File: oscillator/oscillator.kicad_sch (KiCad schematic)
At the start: 32 parts, among them SW1 LFO Switch, U1 AS3340-custom, U2 TL074, U3 TL072

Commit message: Improve oscillator bass
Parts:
- C3: value 1nF -> 4.7nF
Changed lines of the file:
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@@
 		)
 	)
-	(text_box "Switch to toggle between an audio frequency oscillator and a low-frequency oscillator."
+	(text_box "Switch to toggle between an audio frequency oscillator and a low-frequency oscillator.\n\nHigher capacitance means a lower frequency. The design this is based off used lower valued capacitors here but I found these values to produce a more useful low-end of the frequency spectrum produced by the oscillator."
 		(exclude_from_sim no)
 		(at 246.38 115.57 0)
-		(size 24.13 12.7)
+		(size 24.13 38.1)
 		(stroke
 			(width 0)
@@
 			)
 		)
-		(property "Value" "1nF"
-			(at 240.03 142.748 90)
+		(property "Value" "4.7nF"
+			(at 240.03 143.51 90)
 			(effects
 				(font

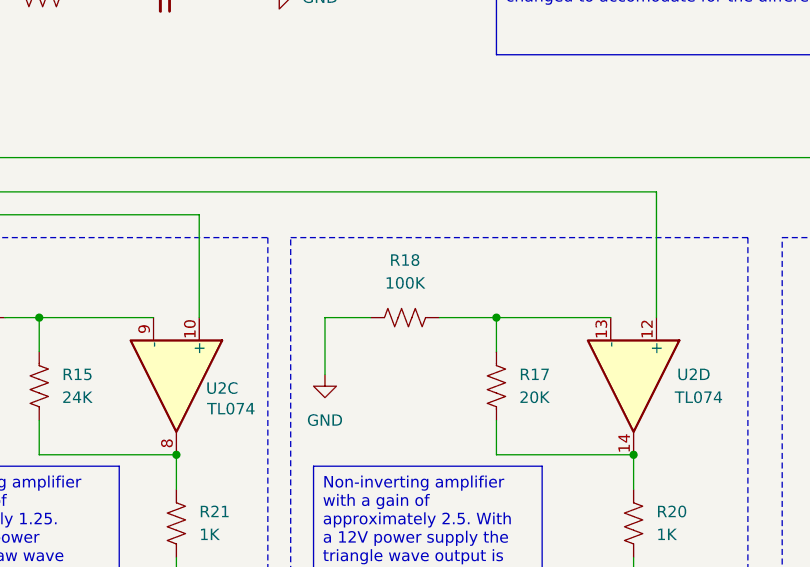
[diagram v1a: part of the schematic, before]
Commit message: Fix typo in oscillator
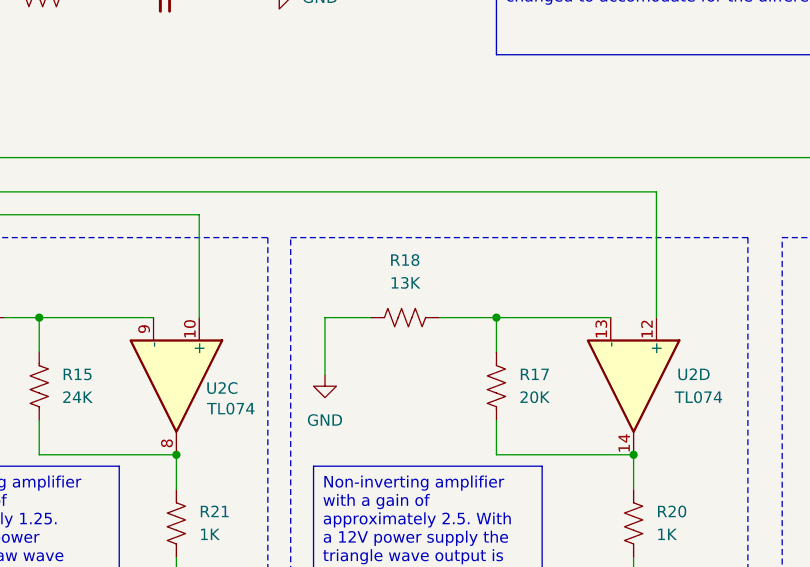
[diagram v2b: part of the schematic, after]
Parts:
- R18: value 100K -> 13K
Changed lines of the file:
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@@
 			)
 		)
-		(property "Value" "100K"
+		(property "Value" "13K"
 			(at 181.61 116.84 90)
 			(effects

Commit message: Fix some tyos in oscillator
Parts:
- removed C2: 10nF, symbol Device:C_Small
- removed U3: TL072, symbol Amplifier_Operational:TL072
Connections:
- net GND: now also R13.2

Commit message: Change oscillator resistor to match AS3340 notes
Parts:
- R4: value 10K -> 51K
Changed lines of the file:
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@@
+		)
+	)
+	(text_box "For R4 (between the pulse output and ground), apparently the AS3340 works better with a 51k resistor here rather than the 10k needed by the CEM3340."
+		(exclude_from_sim no)
+		(at 15.24 50.8 0)
+		(size 22.86 19.05)
+		(stroke
+			(width 0)
+			(type default)
+		)
+		(fill
+			(type none)
+		)
+		(effects
+			(font
+				(size 1.27 1.27)
+			)
+			(justify left top)
 		)
 	)
@@
 			)
 		)
-		(property "Value" "10K"
+		(property "Value" "51K"
 			(at 61.214 80.01 90)
 			(effects
